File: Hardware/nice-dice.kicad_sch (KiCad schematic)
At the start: 22 parts, among them J1 AVR-ISP-6, SW1 SW_Push, SW2 SW_DIP_x01, U1 ATtiny13A-SS, U2 74HC595

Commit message: Начало работы над  печатной платойплатой
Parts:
- BT1: footprint (none) -> Battery:BatteryHolder_Keystone_3002_1x2032
- D1, D2, D3, D4, D5, D6, D7: footprint (none) -> LED_THT:LED_D3.0mm
- J1: footprint (none) -> Connector_PinSocket_2.54mm:PinSocket_2x03_P2.54mm_Vertical
- R1, R2, R3, R4, R5, R6, R7, R8, R9: footprint (none) -> Resistor_SMD:R_1206_3216Metric_Pad1.30x1.75mm_HandSolder
- SW1: footprint (none) -> Button_Switch_SMD:SW_Push_1P1T_NO_6x6mm_H9.5mm
- SW2: footprint (none) -> Button_Switch_SMD:SW_DIP_SPSTx01_Slide_Copal_CHS-01B_W7.62mm_P1.27mm
- U2: footprint (none) -> Package_SO:SOIC-16_3.9x9.9mm_P1.27mm

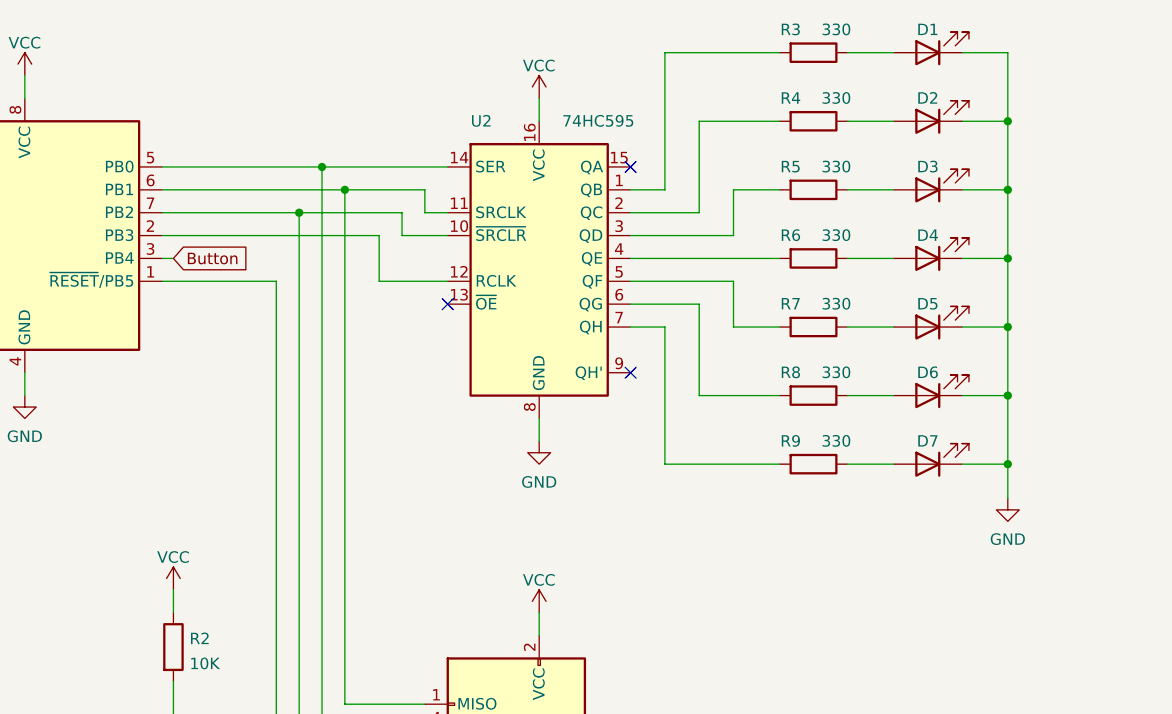
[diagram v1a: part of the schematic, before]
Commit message: Изменены подключения OE и SRCLR
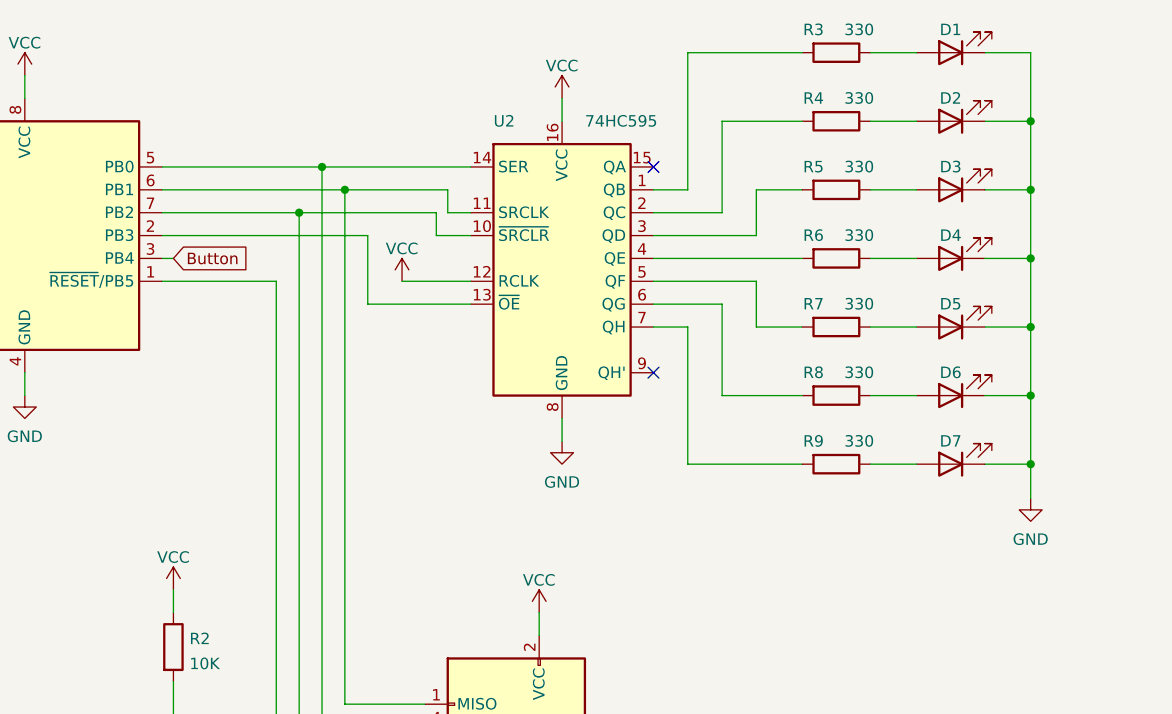
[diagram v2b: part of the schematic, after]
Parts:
- J1: footprint Connector_PinSocket_2.54mm:PinSocket_2x03_P2.54mm_Vertical -> Connector_PinHeader_2.54mm:PinHeader_2x03_P2.54mm_Vertical
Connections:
- net VCC: now also U2.12 (RCLK)
- net at U1.2 (PB3): now also U2.13 (~{OE}); no longer U2.12 (RCLK)
- no-connect marks 3 -> 2
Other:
- moved on the sheet: D1, D2, D3, D4, D5, D6, D7, R3, R4, R5, R6, R7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

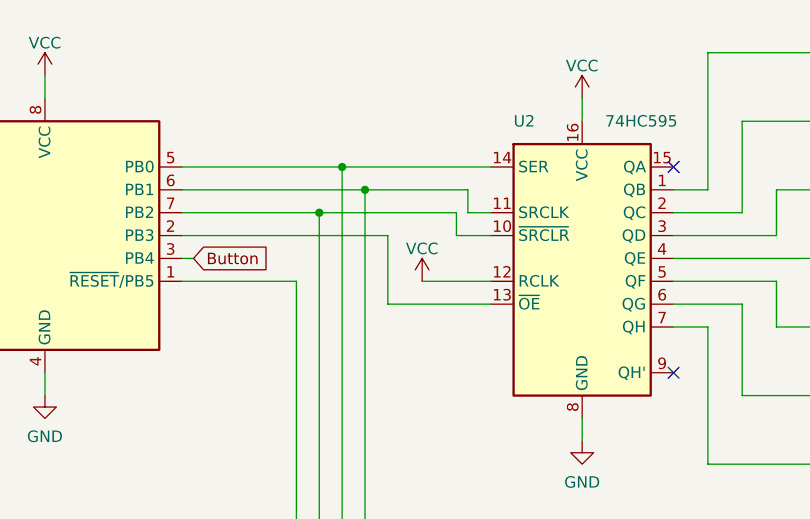
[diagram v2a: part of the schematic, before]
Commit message: Изменены подключения OE и SRCLR сдвигового регистра
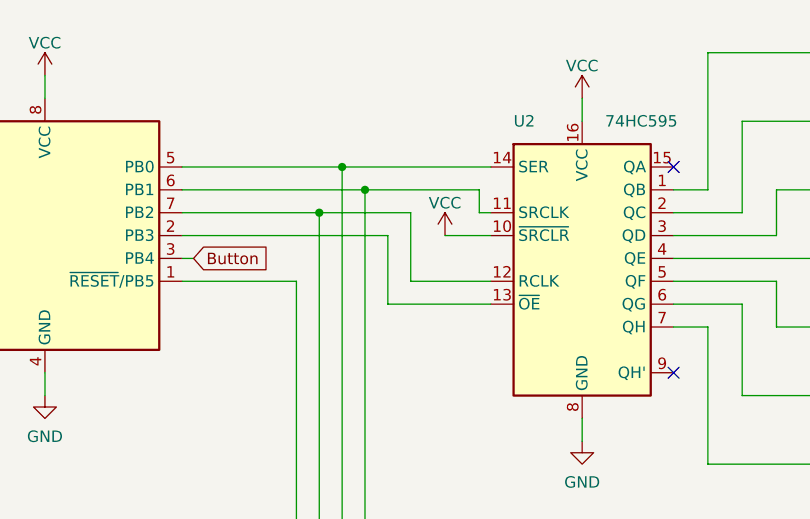
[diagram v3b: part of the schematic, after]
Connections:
- net VCC: now also U2.10 (~{SRCLR}); no longer U2.12 (RCLK)
- net at J1.3 (SCK), U1.7 (PB2): now also U2.12 (RCLK); no longer U2.10 (~{SRCLR})
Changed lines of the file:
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@@
+    (stroke (width 0) (type default) (color 0 0 0 0))
+  )
+  (wire (pts (xy 156.21 58.42) (xy 161.29 58.42))
     (stroke (width 0) (type default) (color 0 0 0 0))
   )
@@
     (stroke (width 0) (type default) (color 0 0 0 0))
   )
-  (wire (pts (xy 158.75 55.88) (xy 161.29 55.88))
+  (wire (pts (xy 160.02 55.88) (xy 161.29 55.88))
     (stroke (width 0) (type default) (color 0 0 0 0))
   )
@@
     (stroke (width 0) (type default) (color 0 0 0 0))
   )
-  (wire (pts (xy 158.75 53.34) (xy 158.75 55.88))
+  (wire (pts (xy 160.02 53.34) (xy 160.02 55.88))
+    (stroke (width 0) (type default) (color 0 0 0 0))
+  )
+  (wire (pts (xy 152.4 55.88) (xy 152.4 63.5))
     (stroke (width 0) (type default) (color 0 0 0 0))
   )
@@
     (stroke (width 0) (type default) (color 0 0 0 0))
   )
-  (wire (pts (xy 142.24 55.88) (xy 157.48 55.88))
-    (stroke (width 0) (type default) (color 0 0 0 0))
-  )
-  (wire (pts (xy 157.48 58.42) (xy 161.29 58.42))
+  (wire (pts (xy 142.24 55.88) (xy 152.4 55.88))
     (stroke (width 0) (type default) (color 0 0 0 0))
   )
@@
     (stroke (width 0) (type default) (color 0 0 0 0))
   )
-  (wire (pts (xy 153.67 63.5) (xy 161.29 63.5))
+  (wire (pts (xy 152.4 63.5) (xy 161.29 63.5))
     (stroke (width 0) (type default) (color 0 0 0 0))
   )
@@
     (stroke (width 0) (type default) (color 0 0 0 0))
   )
-  (wire (pts (xy 157.48 55.88) (xy 157.48 58.42))
-    (stroke (width 0) (type default) (color 0 0 0 0))
-  )
   (wire (pts (xy 193.04 63.5) (xy 193.04 68.58))
     (stroke (width 0) (type default) (color 0 0 0 0))
@@
     (stroke (width 0) (type default) (color 0 0 0 0))
   )
-  (wire (pts (xy 147.32 53.34) (xy 158.75 53.34))
+  (wire (pts (xy 147.32 53.34) (xy 160.02 53.34))
     (stroke (width 0) (type default) (color 0 0 0 0))
   )
@@
     (pin "1")
   )
-  (symbol (lib_id "power:VCC") (at 153.67 63.5 0) (unit 1)
-    (in_bom yes) (on_board yes) (fields_autoplaced)
-    (property "Reference" "#PWR?" (id 0) (at 153.67 67.31 0)
-      (effects (font (size 1.27 1.27)) hide)
-    )
-    (property "Value" "VCC" (id 1) (at 153.67 59.8955 0))
-    (property "Footprint" "" (id 2) (at 153.67 63.5 0)
-      (effects (font (size 1.27 1.27)) hide)
-    )
-    (property "Datasheet" "" (id 3) (at 153.67 63.5 0)
-      (effects (font (size 1.27 1.27)) hide)
-    )
+  (symbol (lib_id "power:VCC") (at 156.21 58.42 0) (unit 1)
+    (in_bom yes) (on_board yes) (fields_autoplaced)
+    (property "Reference" "#PWR?" (id 0) (at 156.21 62.23 0)
+      (effects (font (size 1.27 1.27)) hide)
+    )
+    (property "Value" "VCC" (id 1) (at 156.21 54.8155 0))
+    (property "Footprint" "" (id 2) (at 156.21 58.42 0)
+      (effects (font (size 1.27 1.27)) hide)
+    )
+    (property "Datasheet" "" (id 3) (at 156.21 58.42 0)
+      (effects (font (size 1.27 1.27)) hide)
+    )

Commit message: Добавлена подтяжка выхода OE сдвигового регистра
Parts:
- added R3: 10K, Resistor_SMD:R_1206_3216Metric_Pad1.30x1.75mm_HandSolder, symbol Device:R
- BT1: footprint Battery:BatteryHolder_Keystone_3002_1x2032 -> Library:Battery_Holder_20mm
- renumbered R9 to R10, R3 to R4, R4 to R5, R5 to R6, R6 to R7, R7 to R8, R8 to R9
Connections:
- net VCC: now also R3.1
- net at U1.2 (PB3), U2.13 (~{OE}): now also R3.2
